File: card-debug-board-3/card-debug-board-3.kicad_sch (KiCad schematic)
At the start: 87 parts, among them J1 USB4105-GF-A, J2 USB4105-GF-A, J3 Conn_01x05, J4 5040501291, J5 2-1734592-0, Q1 PMV450ENEAR, SW1 B3F-1000, SW2 PCM13SMTR, SW3 B3F-1000, SW4 78RB02T, U1 MIC5205-3.3YM5, U2 W25Q16JVSS, U3 RP2040, U4 74AUP1G17, U5 74AUP1G17, U6 IP4234CZ6,125, U7 IP4234CZ6,125, Y1 12 MHz

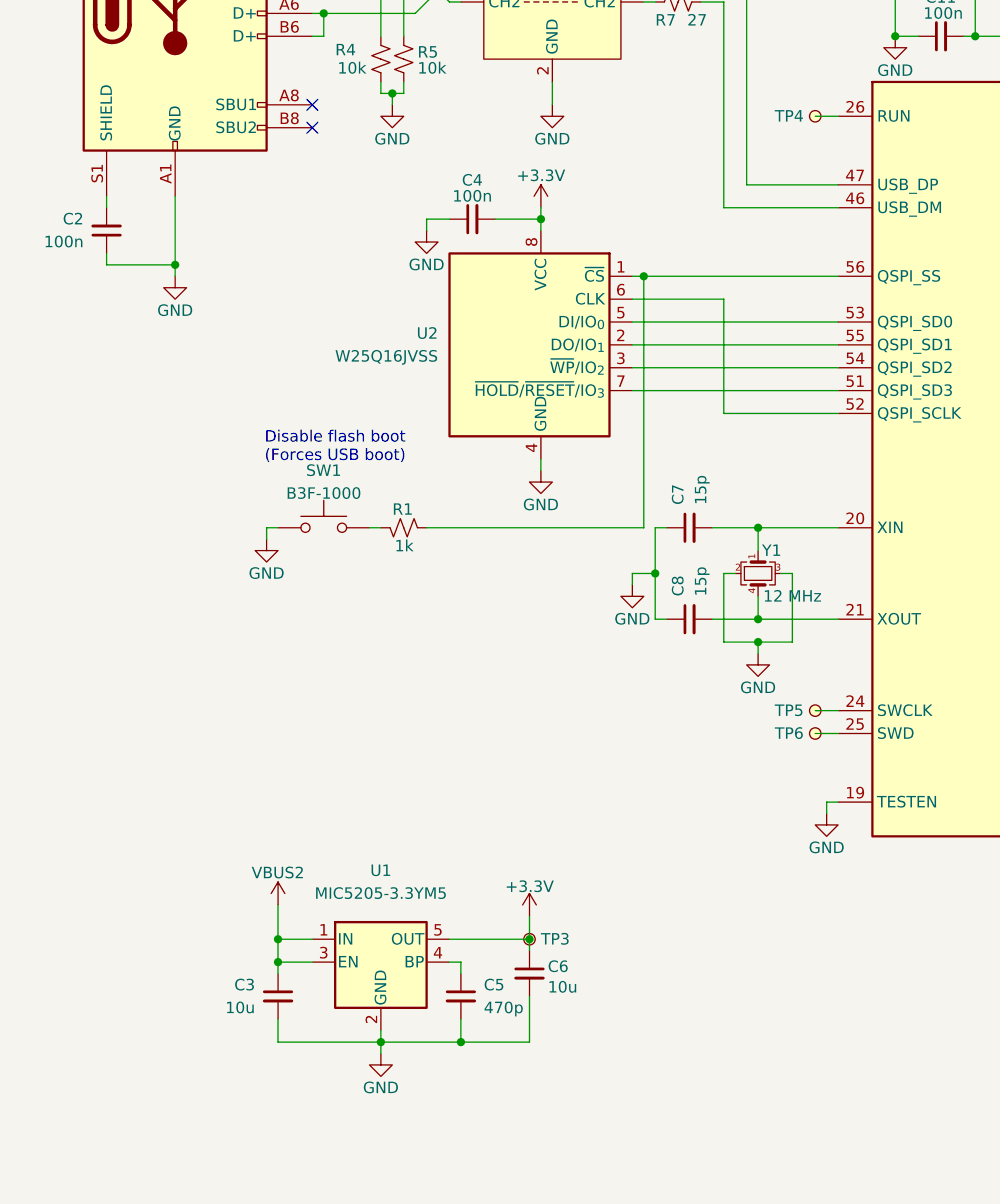
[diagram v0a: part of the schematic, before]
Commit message: More layout.
Also added 1k resistor to crystal, starting to move things around for final layout.
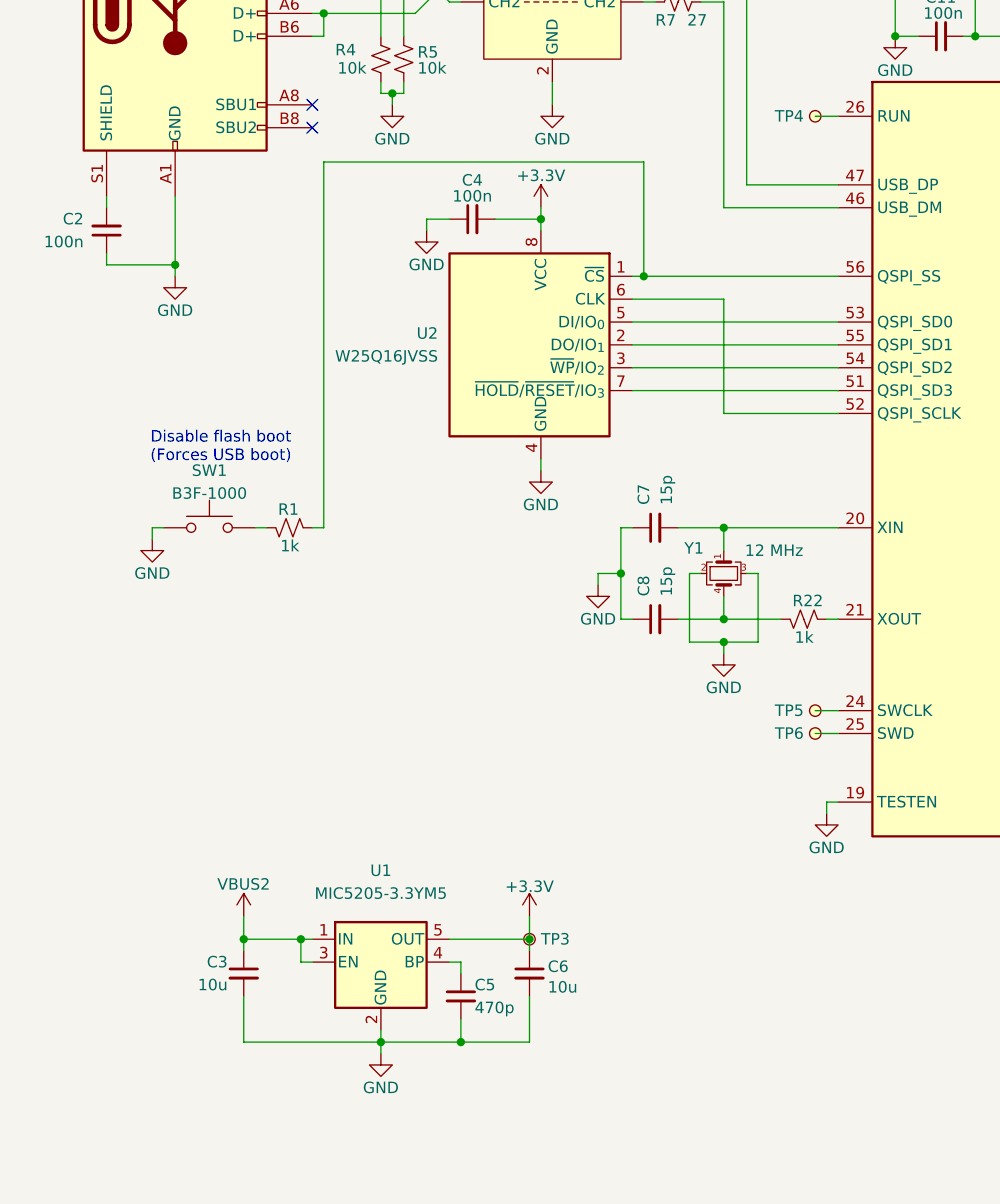
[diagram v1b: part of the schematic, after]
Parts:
- added R22: 1k, oresat-passives:0603-C-NOSILK, symbol Device:R_Small_US
- C1, C10, C11, C12, C13, C14, C15, C16, C17, C18, C19, C2, C20, C21, C4, C5, C7, C8, C9: footprint Capacitor_SMD:C_0603_1608Metric -> oresat-passives:0603-C-NOSILK
- C3, C6: footprint Capacitor_SMD:C_0603_1608Metric -> oresat-passives:0805-C-NOSILK
- R1, R10, R11, R12, R13, R14, R15, R16, R17, R18, R19, R2, R20, R21, R3, R4, R5, R6, R7, R8, R9: footprint Resistor_SMD:R_0603_1608Metric -> oresat-passives:0603-C-NOSILK
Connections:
- net at C8.2, Y1.4: now also R22.1; no longer U3.21 (XOUT)
- new net: R22.2, U3.21 (XOUT)
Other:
- moved on the sheet: C3, C7, C8, R1, SW1, Y1

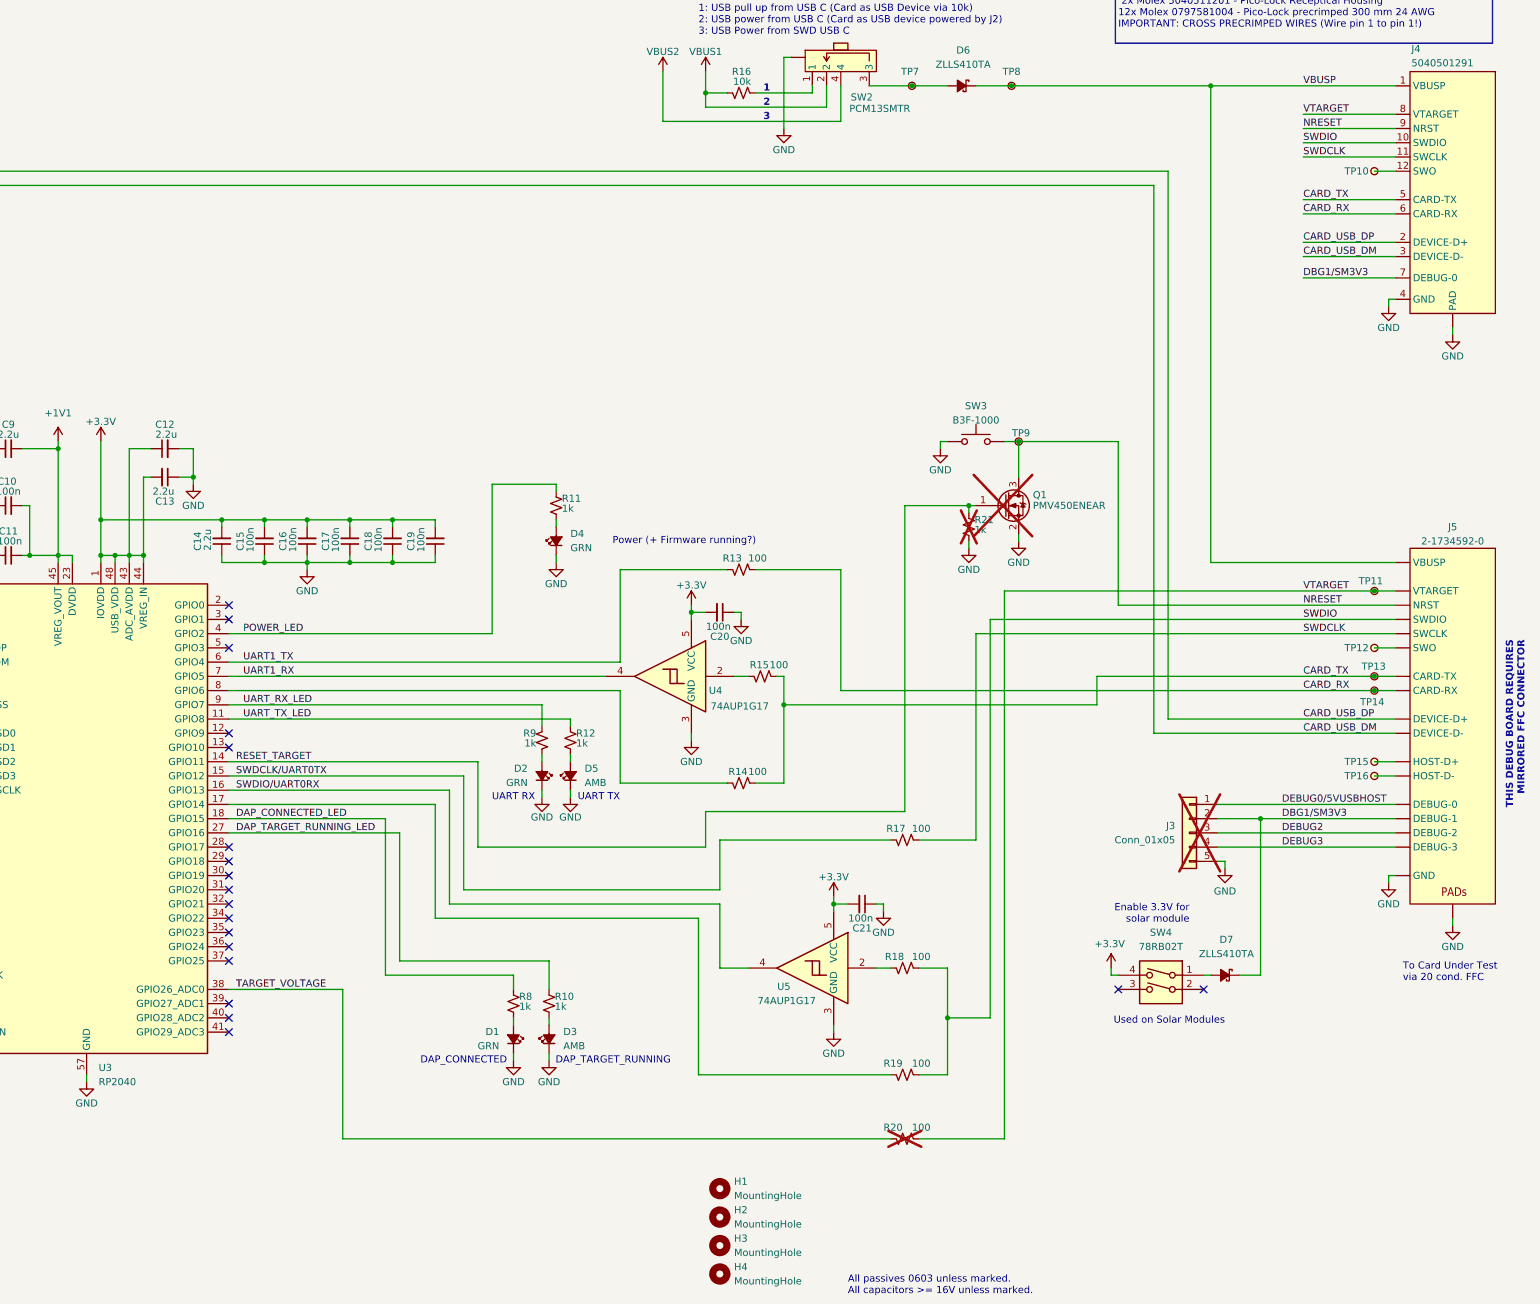
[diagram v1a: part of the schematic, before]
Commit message: Initial Card Debug Board v3
Cleaned up routing, added test points that Pete suggested, routed as best and as quickly as possible!
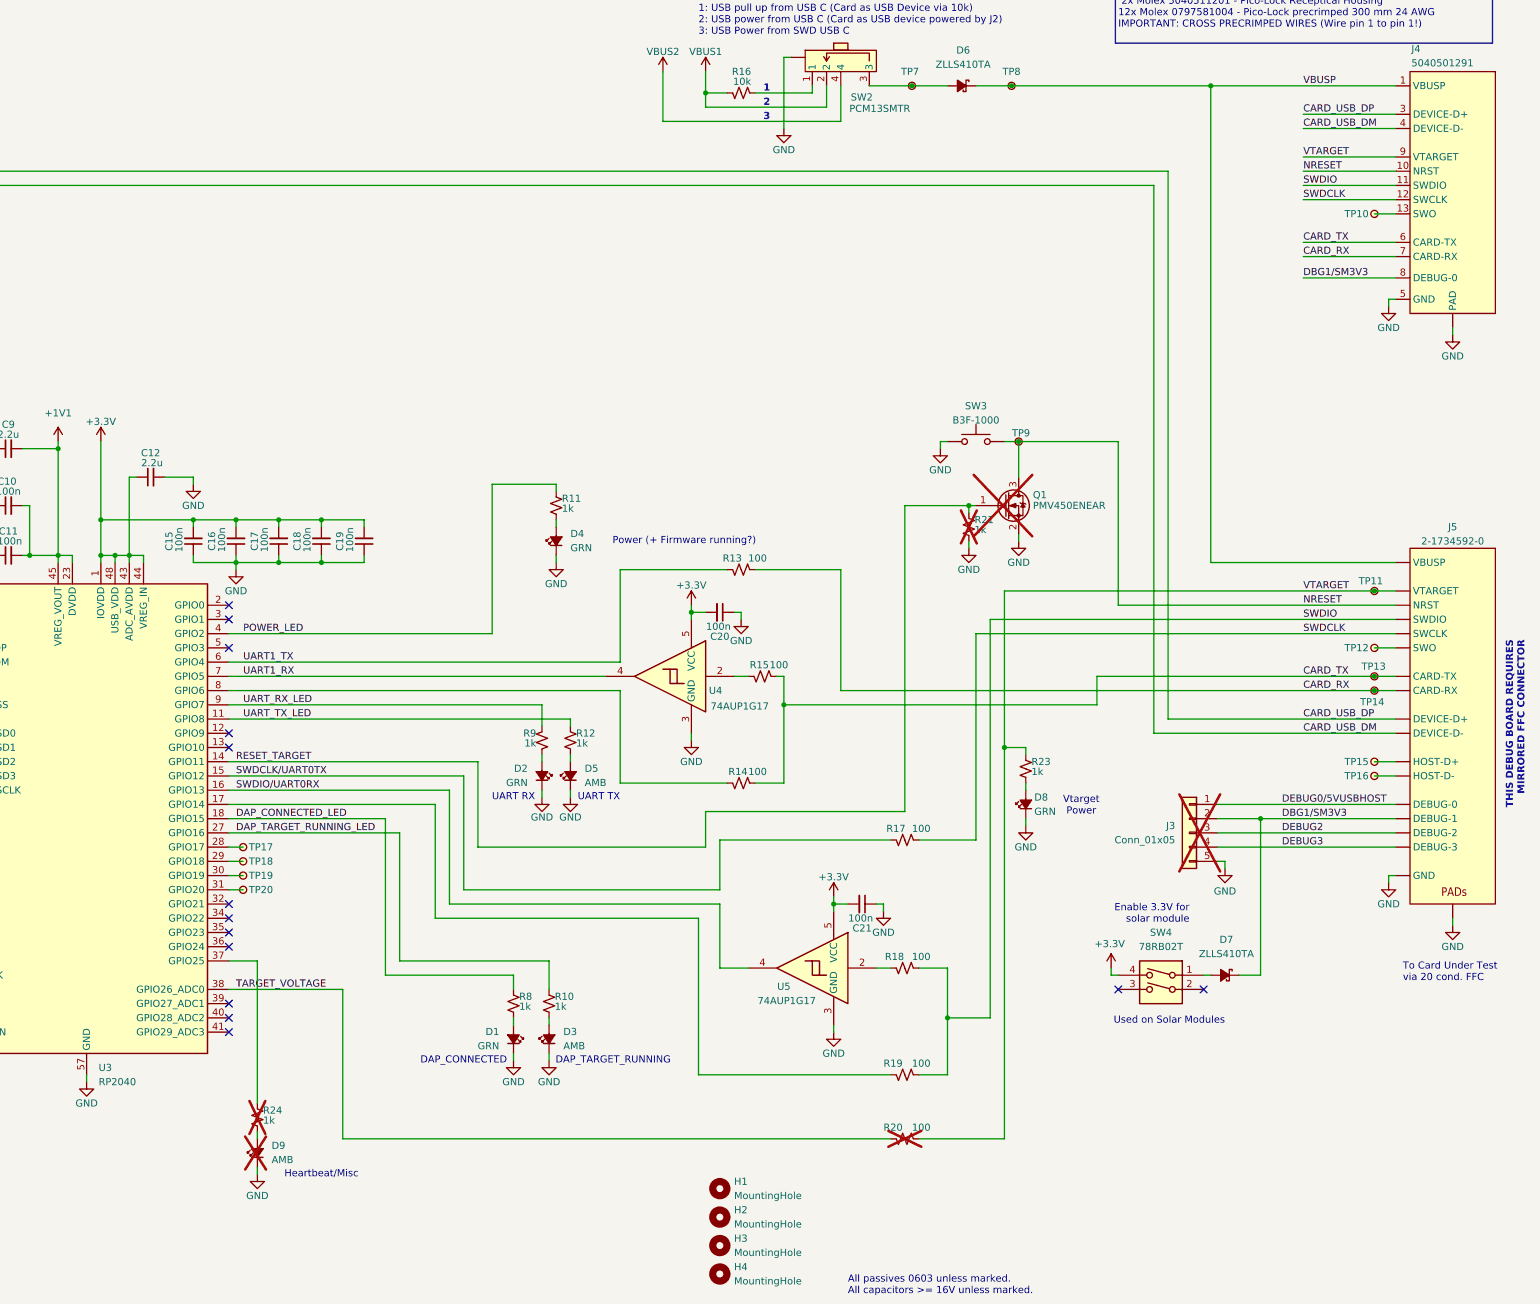
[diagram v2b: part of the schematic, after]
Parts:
- removed C13, C14: 2.2u, oresat-passives:0603-C-NOSILK, symbol Device:C_Small
- added D8: GRN, LED_SMD:LED_0603_1608Metric, symbol Device:LED_Small_Filled
- added D9: AMB, LED_SMD:LED_0603_1608Metric, symbol Device:LED_Small_Filled
- added R23, R24: 1k, oresat-passives:0603-C-NOSILK, symbol Device:R_Small_US
- added TP17, TP18, TP19, TP20: TestPoint-MinTH, oresat-misc:TestPoint-MinTH, symbol oresat-misc:TestPoint-MinTH
- J4: footprint oresat-connectors:J-MOLEX-5040501291 -> oresat-connectors:J-JST-SM14BSHLSTF; DPN WM16219CT-ND -> 455-SM14B-SHLS-TFCT-ND; MFR Molex -> JST; MPN 5040501291 -> SM14B-SHLS-TF
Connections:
- net CARD_RX: now also J4.7 (CARD-RX); no longer J4.6 (CARD-RX)
- net CARD_TX: now also J4.6 (CARD-TX); no longer J4.5 (CARD-TX)
- net CARD_USB_DM: now also J4.4 (DEVICE-D-); no longer J4.3 (DEVICE-D-)
- net CARD_USB_DP: now also J4.3 (DEVICE-D+); no longer J4.2 (DEVICE-D+)
- net DBG1/SM3V3: now also J4.8 (DEBUG-0); no longer J4.7 (DEBUG-0)
- net GND: now also J4.15 (PAD), J4.16 (PAD), J4.5 (GND), D8.1 (K), D9.1 (K); no longer J4.13 (PAD), J4.4 (GND)
- net NRESET: now also J4.10 (NRST); no longer J4.9 (NRST)
- net SWDCLK: now also J4.12 (SWCLK); no longer J4.11 (SWCLK)
- net SWDIO: now also J4.11 (SWDIO); no longer J4.10 (SWDIO)
- net VBUSP: now also J4.2 (VBUSP)
- net VTARGET: now also J4.9 (VTARGET), R23.2; no longer J4.8 (VTARGET)
- net at TP10.1: now also J4.13 (SWO); no longer J4.12 (SWO)
- net at U3.28 (GPIO17): now also TP17.1
- net at U3.29 (GPIO18): now also TP18.1
- net at U3.30 (GPIO19): now also TP19.1
- net at U3.31 (GPIO20): now also TP20.1
- net at U3.37 (GPIO25): now also R24.2
- new net: D8.2 (A), R23.1
- new net: D9.2 (A), R24.1
- no-connect marks 23 -> 18
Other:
- note added: "Heartbeat/Misc"
- note added: "Vtarget Power"
- moved on the sheet: C12, C15, C16, C17, C18, C19, TP10

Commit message: Small fix to create v3.1 (functionally the same as v3.0), updated BOM, and added a README.
The BOM is now officially finished and can be used to order parts. The README now points the Google Doc design notes. Updated the board and schematic to v3.1 just because we found a small error in v3.0 that we should fix ASAP.
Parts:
- C1, C10, C11, C15, C16, C17, C18, C19, C2, C20, C21, C4: DIS (none) -> DigiKey; DPN (none) -> 587-3472-1-ND; MFR (none) -> Taiyo Yuden; MPN (none) -> TMK107BJ104KAHT
- C12, C9: DIS (none) -> DigiKey; DPN (none) -> 587-4929-1-ND; MFR (none) -> Taiyo Yuden; MPN (none) -> TMK107BBJ225MAHT
- C3, C6: DIS (none) -> DIgiKey; DPN (none) -> 490-GRT21BC71E106KE13LCT-ND; MFR (none) -> Murata Electronics; MPN (none) -> GRT21BC71E106KE13L
- C5: DIS (none) -> DigiKey; DPN (none) -> 1276-6700-1-ND; MFR (none) -> Samsung; MPN (none) -> CL10B471KC8WPNC
- D1, D2, D4, D8: DIS (none) -> DigiKey; DPN (none) -> 732-150060GS75020CT-ND; MFR (none) -> Wurth; MPN (none) -> 150060GS75020
- D3, D5: DIS (none) -> DigiKey; DPN (none) -> 732-150060AS75000CT-ND; MFR (none) -> Wurth; MPN (none) -> 150060AS75000
- R1, R10, R11, R12, R22, R23, R8, R9: DIS (none) -> DigiKey; DPN (none) -> RMCF0603FT1K00CT-ND; MFR (none) -> Stackpole Electronics Inc; MPN (none) -> RMCF0603FT1K00
- R13, R14, R15, R17, R18, R19: DIS (none) -> DigiKey; DPN (none) -> RMCF0603FT100RCT-ND; MFR (none) -> Stackpole Electronics Inc; MPN (none) -> RMCF0603FT100R
- R16, R2, R3, R4, R5: DIS (none) -> DigiKey; DPN (none) -> RMCF0603FT10K0CT-ND; MFR (none) -> Stackpole Electronics Inc; MPN (none) -> RMCF0603FT10K0
- R6, R7: DIS (none) -> DigiKey; DPN (none) -> RMCF0603FT27R0CT-ND; MFR (none) -> Stackpole Electronics Inc; MPN (none) -> RMCF0603FT27R0
